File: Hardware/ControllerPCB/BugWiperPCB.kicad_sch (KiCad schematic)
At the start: 13 parts, among them J2 1770924, J3 Phoenix_1776508, J6 1824420000, J7 Conn_01x02_Pin

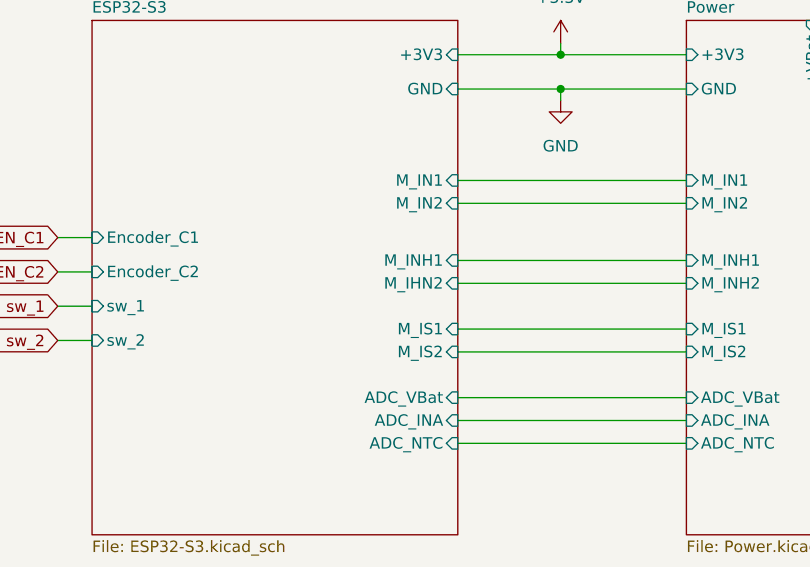
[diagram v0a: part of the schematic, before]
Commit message: Add a micro SD Card slot to the bottom of the controller board
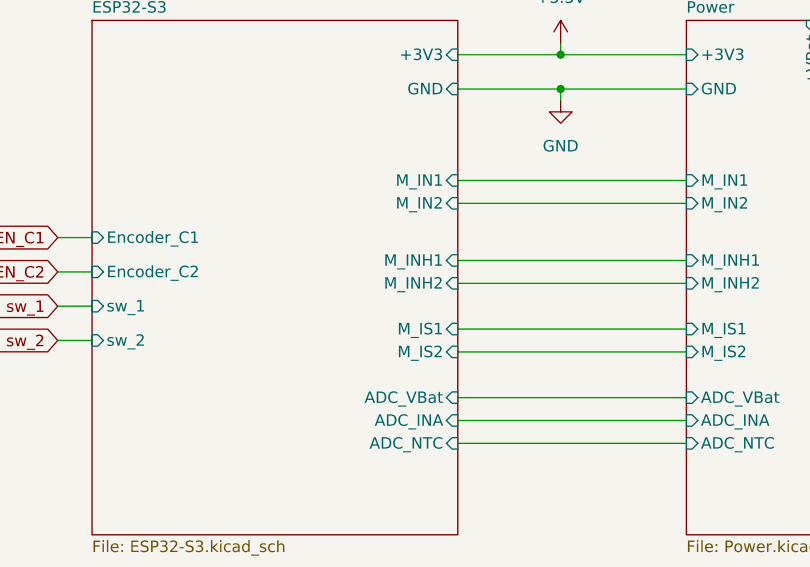
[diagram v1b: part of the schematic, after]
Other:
- sheet ESP32-S3 ports: added M_INH2; removed M_IHN2
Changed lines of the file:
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@@
       (effects (font (size 1.27 1.27)) (justify right))
     )
-    (pin "M_IHN2" input (at 116.84 76.2 0)
+    (pin "M_INH2" input (at 116.84 76.2 0)
       (effects (font (size 1.27 1.27)) (justify right))
     )
